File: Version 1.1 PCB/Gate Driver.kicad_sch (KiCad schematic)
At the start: 22 parts, among them U3 TMC6200-TA-T

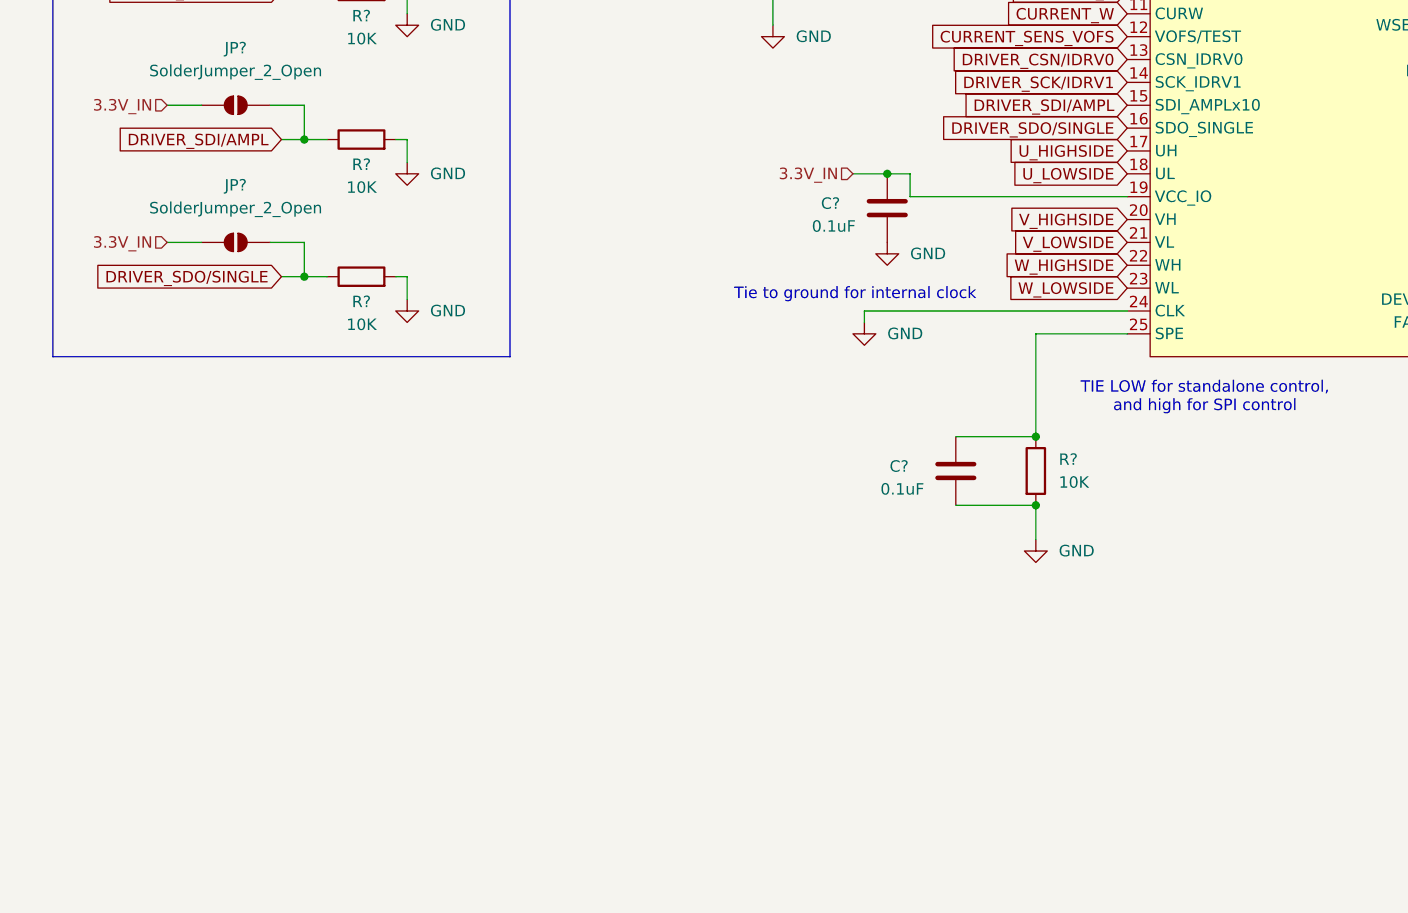
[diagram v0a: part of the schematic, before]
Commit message: Added ESD protection and test pins
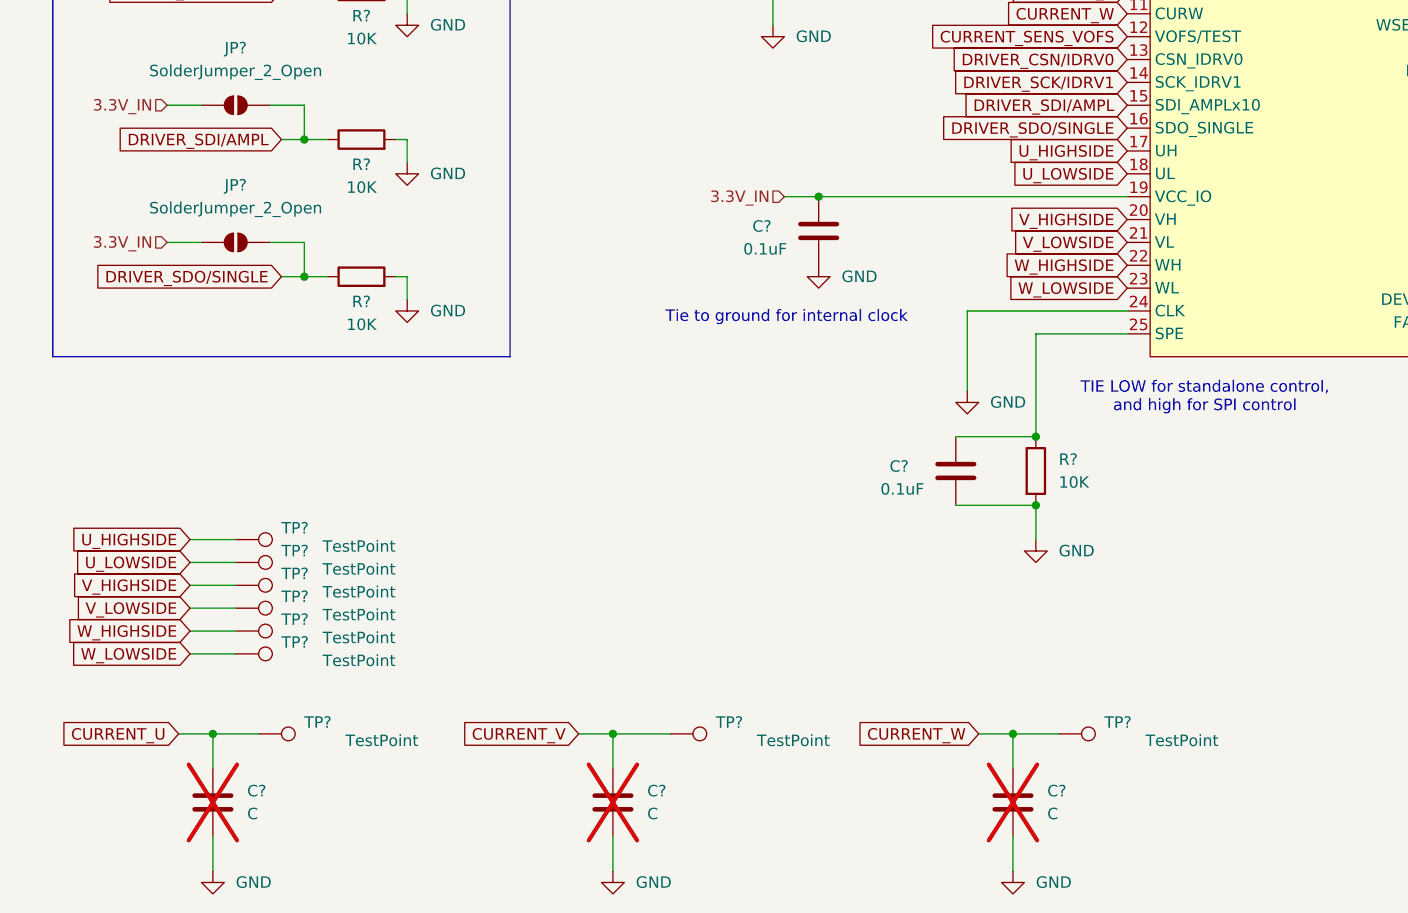
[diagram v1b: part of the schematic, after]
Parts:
- added C? (x3): C, Capacitor_SMD:C_0805_2012Metric_Pad1.18x1.45mm_HandSolder, symbol Device:C
- added TP? (x6): TestPoint, symbol Connector:TestPoint
- added TP? (x3): TestPoint, TestPoint:TestPoint_Pad_D2.0mm, symbol Connector:TestPoint
- JP? (x4): footprint (none) -> Jumper:SolderJumper-2_P1.3mm_Open_TrianglePad1.0x1.5mm
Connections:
- net CURRENT_U: now also C?.1, TP?.1
- net CURRENT_V: now also C?.1, TP?.1
- net CURRENT_W: now also C?.1, TP?.1
- net GND: now also C?.2, C?.2, C?.2
- net U_HIGHSIDE: now also TP?.1
- net U_LOWSIDE: now also TP?.1
- net V_HIGHSIDE: now also TP?.1
- net V_LOWSIDE: now also TP?.1
- net W_HIGHSIDE: now also TP?.1
- net W_LOWSIDE: now also TP?.1
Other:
- moved on the sheet: C?

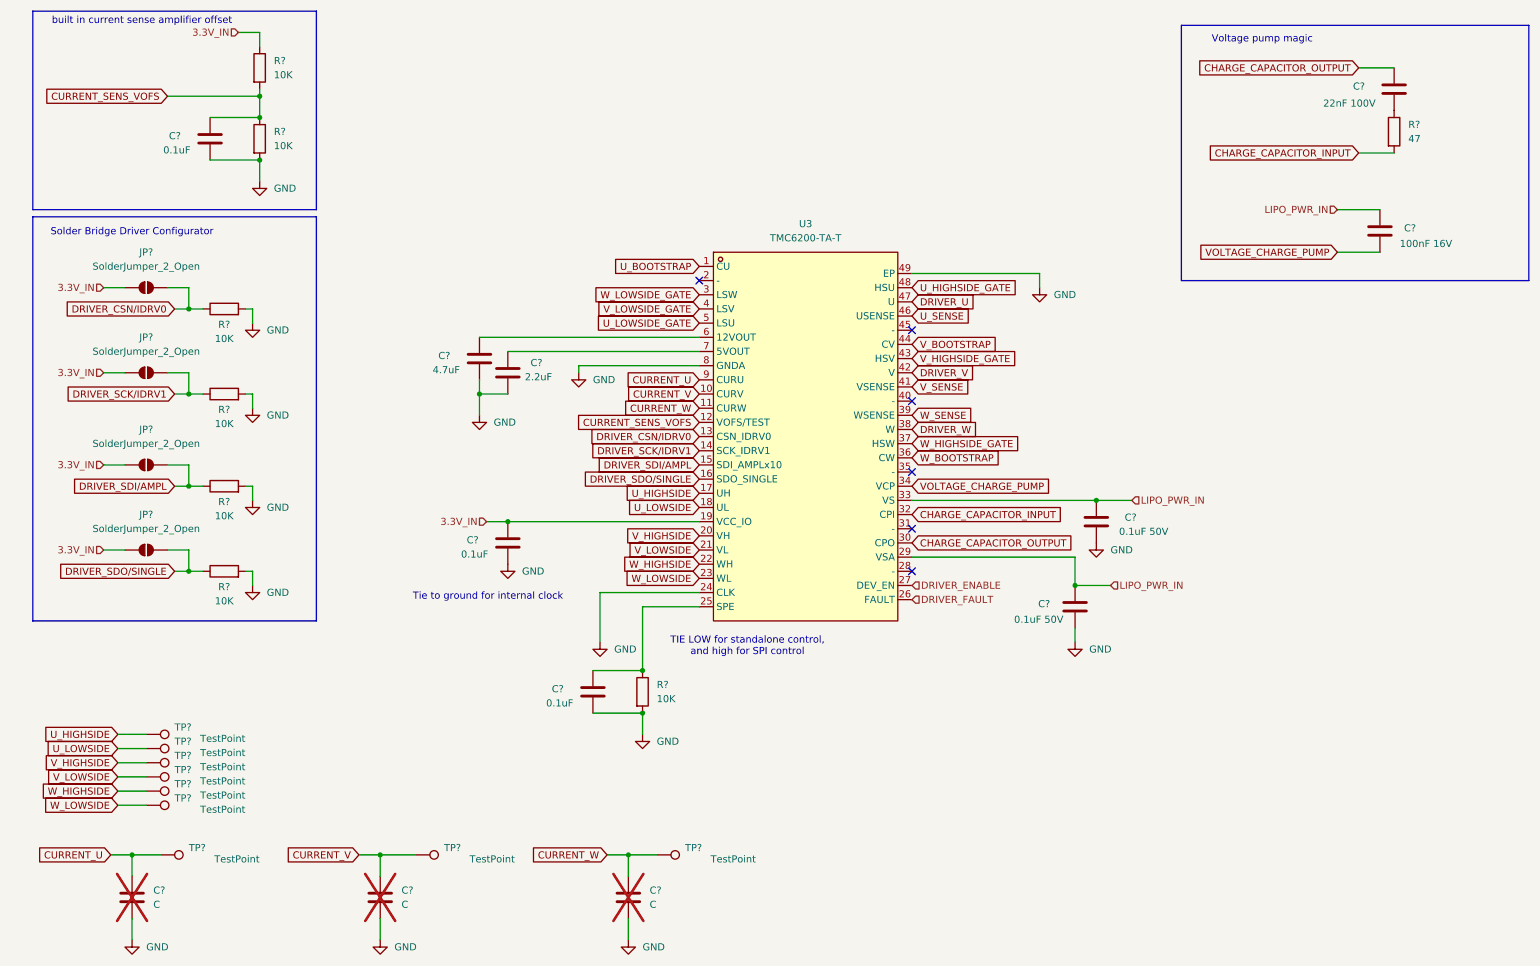
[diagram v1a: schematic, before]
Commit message: began part placement
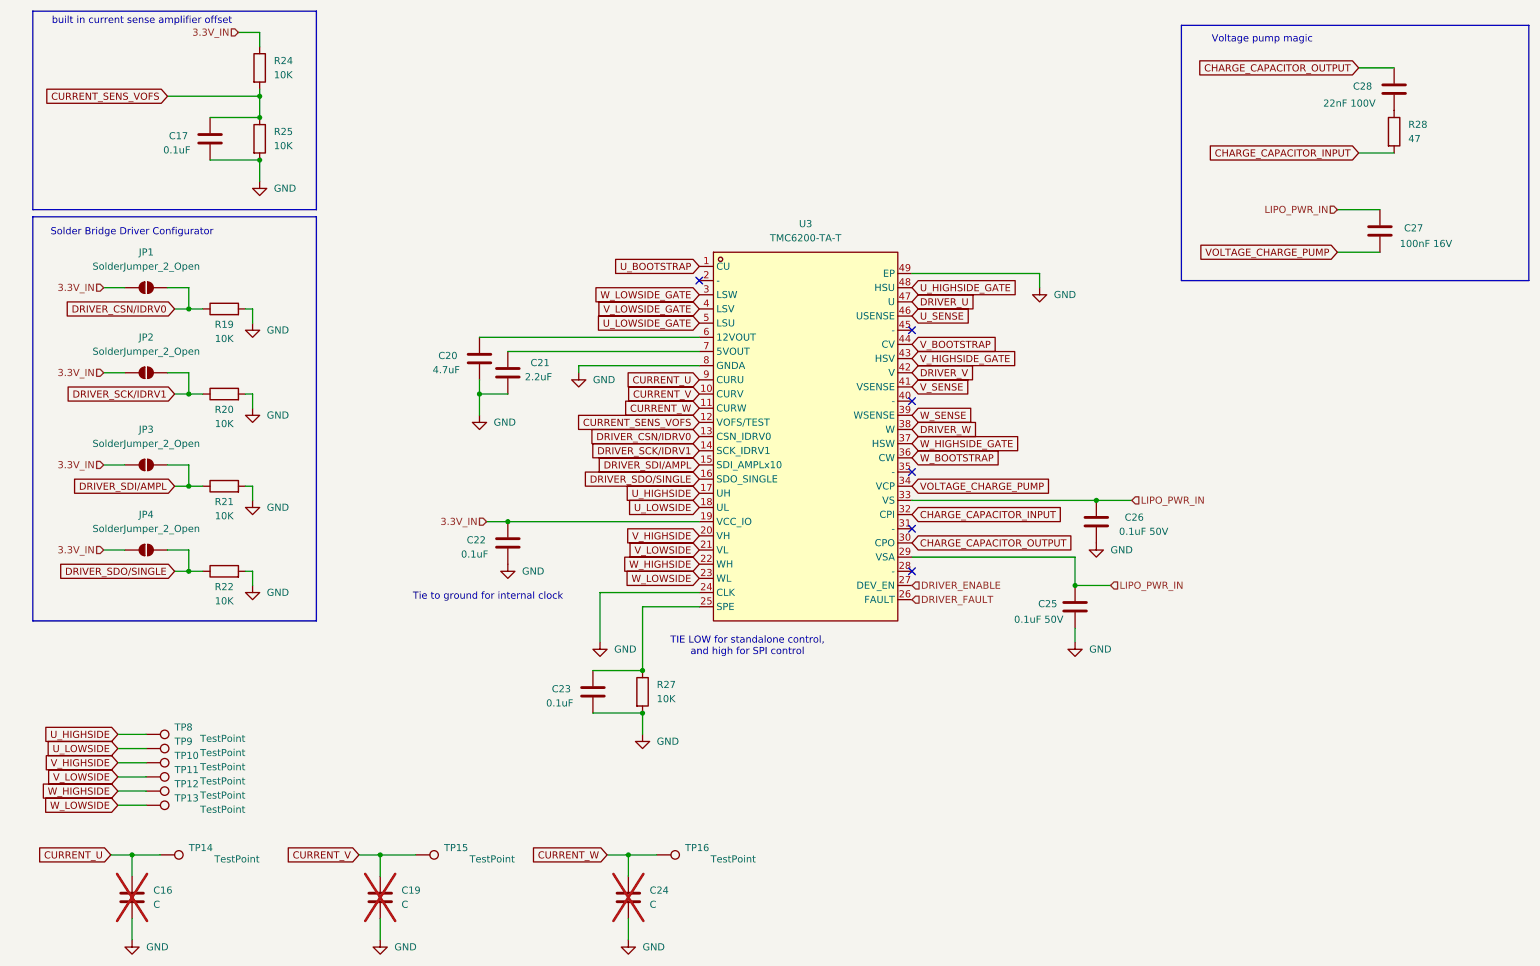
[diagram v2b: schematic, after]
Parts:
- C17, C20, C21, C22, C23, C25, C26, C27, C28: renamed from C?; footprint (none) -> Capacitor_SMD:C_0805_2012Metric_Pad1.18x1.45mm_HandSolder
- R19, R20, R21, R22, R24, R25, R27, R28: renamed from R?; footprint (none) -> Resistor_SMD:R_0805_2012Metric_Pad1.20x1.40mm_HandSolder
- TP10, TP11, TP12, TP13, TP8, TP9: renamed from TP?; footprint (none) -> TestPoint:TestPoint_Pad_D2.0mm
- gave numbers to parts that had none: 10

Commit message: Completed Placement of Parts
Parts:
- TP14, TP15, TP16: footprint TestPoint:TestPoint_Pad_D2.0mm -> easyeda2kicad:SMD_RH-5015
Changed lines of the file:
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@@
 			)
 		)
-		(property "Footprint" "TestPoint:TestPoint_Pad_D2.0mm"
+		(property "Footprint" "easyeda2kicad:SMD_RH-5015"
 			(at 82.55 170.18 0)
 			(effects
@@
 			)
 		)
-		(property "Footprint" "TestPoint:TestPoint_Pad_D2.0mm"
+		(property "Footprint" "easyeda2kicad:SMD_RH-5015"
 			(at 36.83 170.18 0)
 			(effects
@@
 			)
 		)
-		(property "Footprint" "TestPoint:TestPoint_Pad_D2.0mm"
+		(property "Footprint" "easyeda2kicad:SMD_RH-5015"
 			(at 125.73 170.18 0)
 			(effects
